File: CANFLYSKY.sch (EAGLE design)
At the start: 47 parts, among them J1 USB_B_PTH, SW1 SWITCH-DPDT3, U1 MCP2551, X1 INPUT, X2 OUTPUT

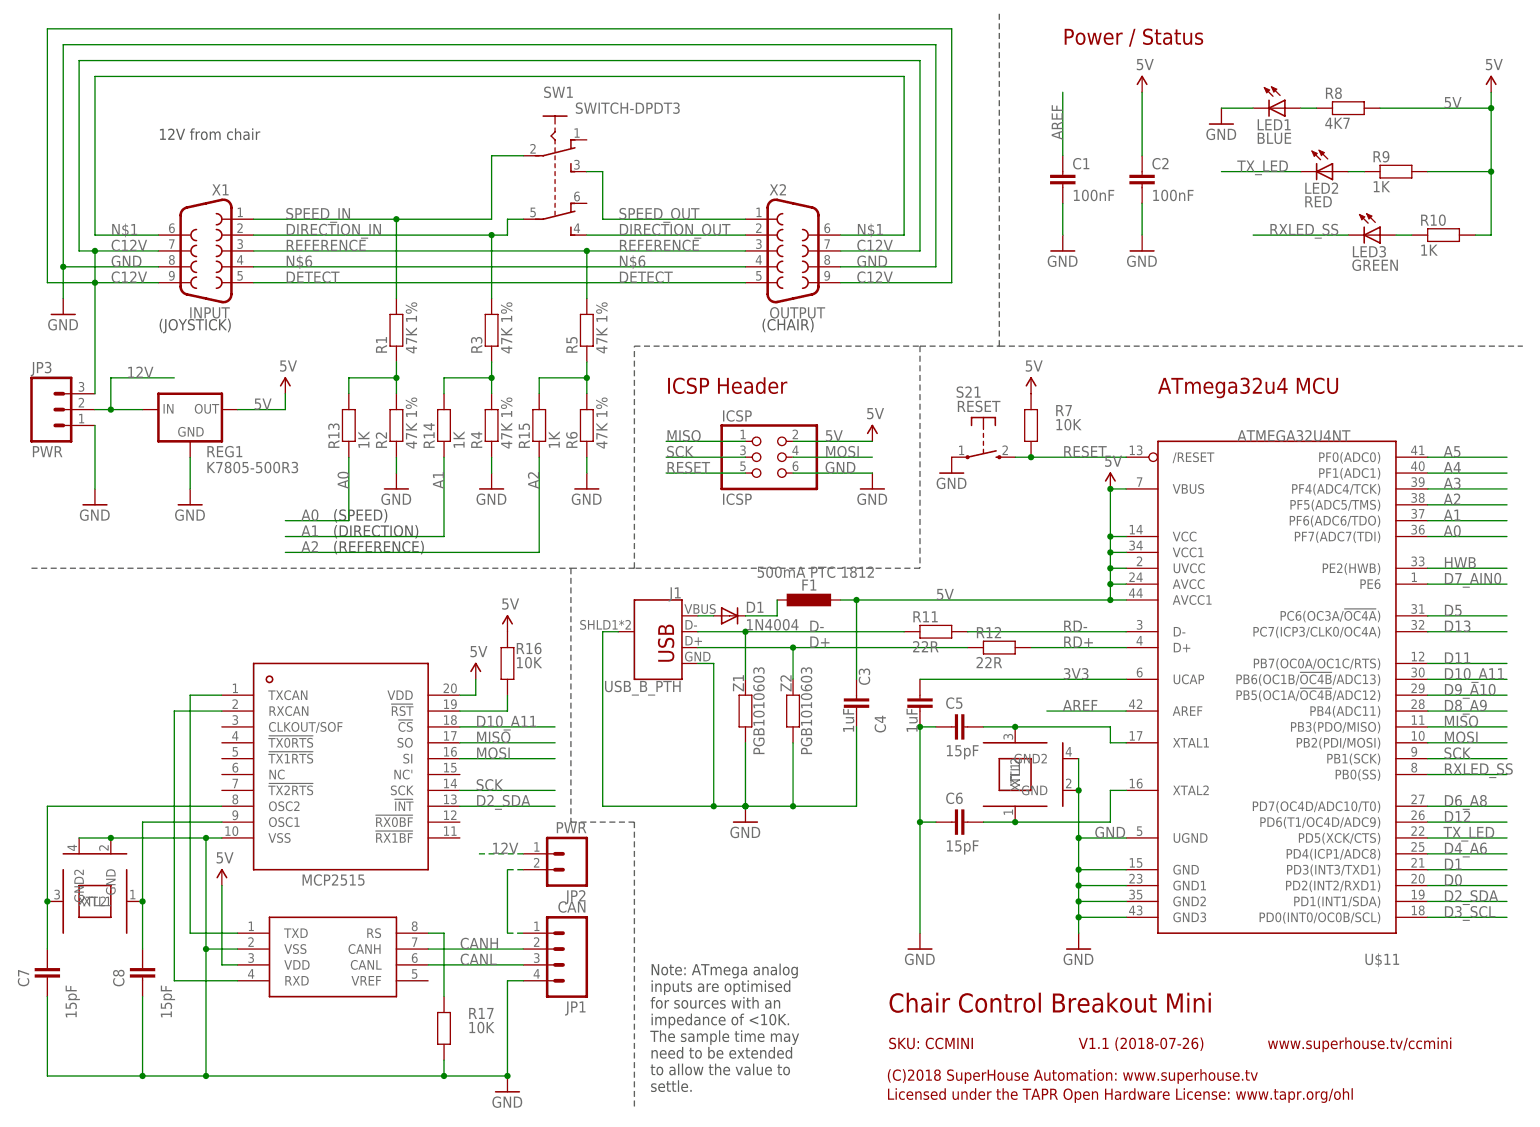
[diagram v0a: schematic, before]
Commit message: Removed unnecessary parts
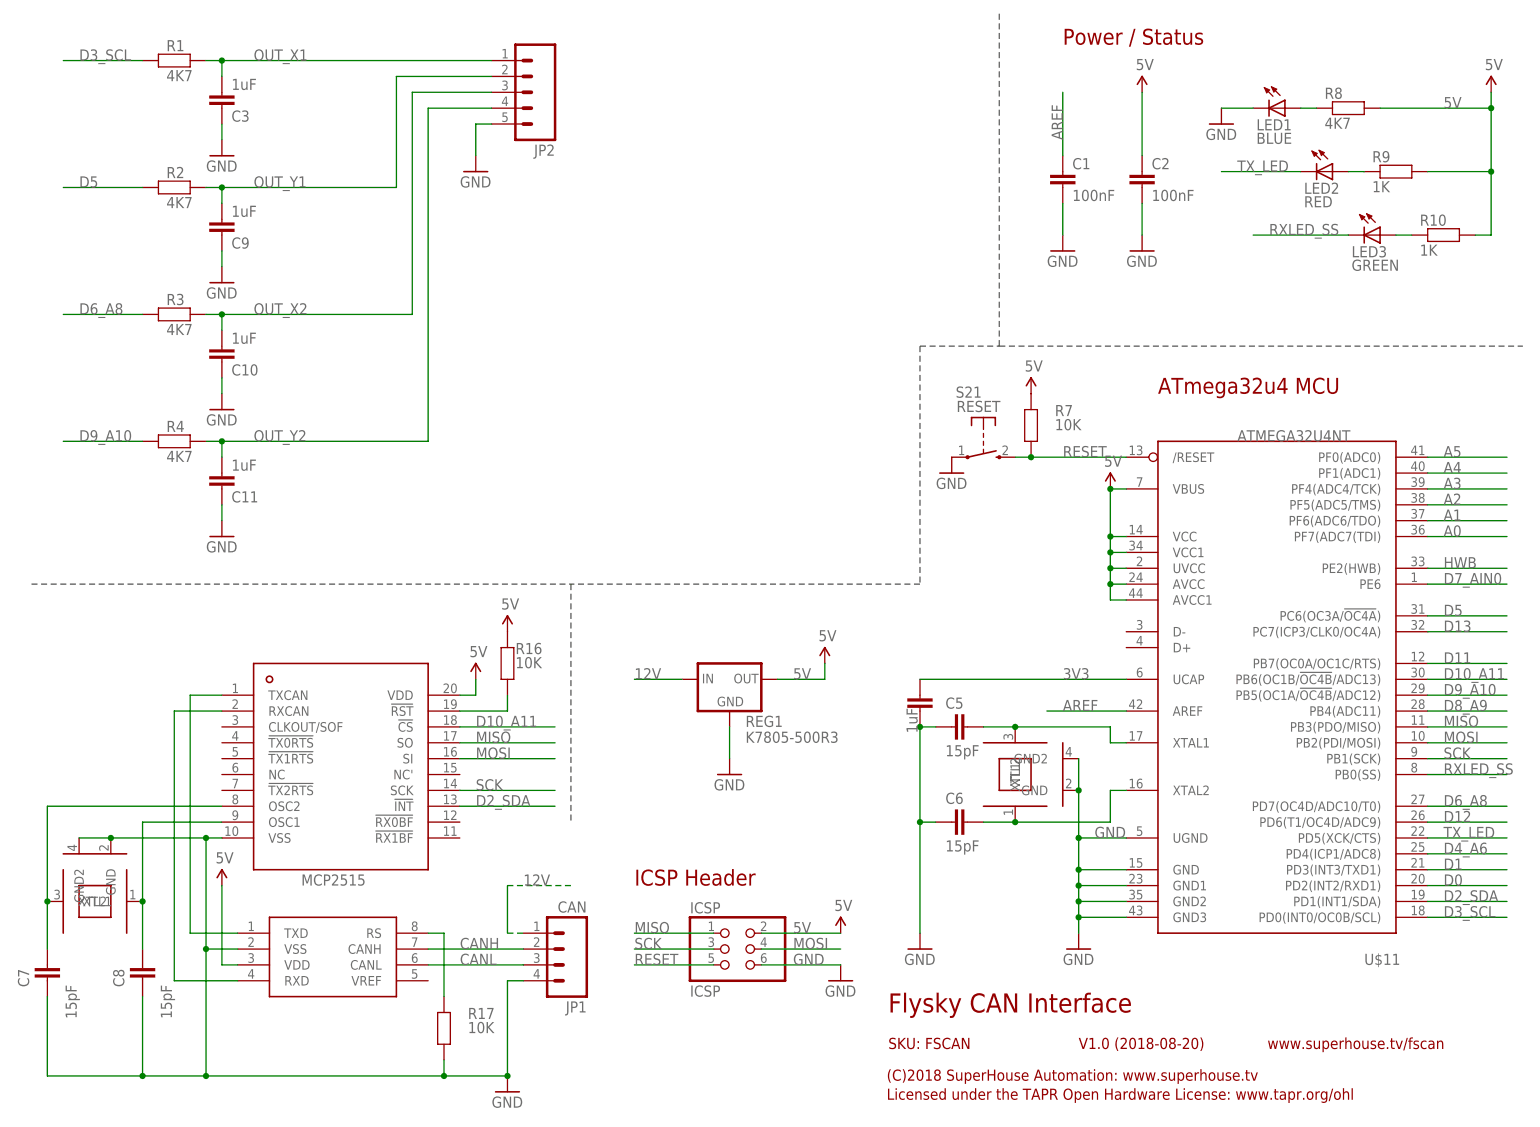
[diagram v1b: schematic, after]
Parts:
- removed D1: 1N4004, freetronics-jon:DIODESMB
- removed F1: 500mA PTC 1812, rcl:L-EUL1812
- removed J1: USB_B_PTH, SparkFun-Connectors:USB_B_PTH
- removed JP3: PWR, freetronics-jon:M03PTH
- removed R11, R12: 22R, freetronics-jon:RESISTOR0603
- removed R13, R14, R15: 1K, freetronics-jon:RESISTOR0603
- removed R5, R6: 47K 1%, freetronics-jon:RESISTOR0603
- removed SW1: SWITCH-DPDT3, freetronics-jon:SWITCH-DPDT3
- removed X1: INPUT, SparkFun-Connectors:DB9MALE
- removed X2: OUTPUT, SparkFun-Connectors:DB9FEMALE
- removed Z1, Z2: PGB1010603, freetronics-master-v1.1:RESISTOR0603
- added C10, C11, C9: 1uF, freetronics-master-v1.1:CAP0603
- JP2: value PWR -> (none); device freetronics-jon:M02PTH -> freetronics-jon:M05PTH
- R1, R2, R3, R4: value 47K 1% -> 4K7; device freetronics-jon:RESISTOR0603 -> freetronics-master-v1.1:RESISTOR0603
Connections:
- removed net C12V: JP3.3, X1.7, X1.9, X2.7, X2.9
- removed net D+: J1.D+, R12.1, Z2.2
- removed net D-: J1.D-, R11.1, Z1.2
- removed net DETECT: X1.5, X2.5
- removed net DIRECTION_IN: R3.2, SW1.5, X1.2
- removed net DIRECTION_OUT: SW1.4, X2.2
- removed net N$1: X1.6, X2.6
- removed net N$15: JP1.1, JP2.2
- removed net N$17: D1.C, F1.1
- removed net N$2: R1.1, R13.2, R2.2
- removed net N$3: R14.2, R3.1, R4.2
- removed net N$4: R15.2, R5.1, R6.2
- removed net N$6: X1.4, X2.4
- removed net RD+: R12.2, U$11.D+
- removed net RD-: R11.2, U$11.D-
- removed net REFERENCE: R5.2, X1.3, X2.3
- removed net SPEED_IN: R1.2, SW1.2, X1.1
- removed net SPEED_OUT: SW1.3, X2.1
- removed net USB+: D1.A, J1.VBUS
- new net OUT_X1: C3.1, JP2.1, R1.2
- new net OUT_X2: C10.1, JP2.3, R3.2
- new net OUT_Y1: C9.1, JP2.2, R2.2
- new net OUT_Y2: C11.1, JP2.4, R4.2
- net 12V: now also JP1.1; no longer JP2.1, JP3.2
- net 5V: no longer C3.1, F1.2
- net A0: no longer R13.1
- net A1: no longer R14.1
- net A2: no longer R15.1
- net D3_SCL: now also R1.1
- net D5: now also R2.1
- net D6_A8: now also R3.1
- net D9_A10: now also R4.1
- net GND: now also C10.2, C11.2, C9.2, JP2.5; no longer J1.GND, J1.SHIELD, JP3.1, R2.1, R4.1, R6.1, X1.8, X2.8, Z1.1, Z2.1
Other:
- note added: "Flysky CAN Interface"
- note added: "SKU: FSCAN"
- note added: "V1.0 (2018-08-20)"
- note added: "www.superhouse.tv/fscan"
- note removed: "(CHAIR)"
- note removed: "(DIRECTION)"
- note removed: "(JOYSTICK)"
- note removed: "(REFERENCE)"
- note removed: "(SPEED)"
- note removed: "12V from chair"
- note removed: "Chair Control Breakout Mini"
- note removed: "Note: ATmega analog inputs are optimised for sources with an impedance of <10K. The sample time may need to be extended to allow the value to settle."
- note removed: "SKU: CCMINI"
- note removed: "V1.1 (2018-07-26)"
- note removed: "www.superhouse.tv/ccmini"
- moved on the sheet: C3, ICSP, R1, R2, R3, R4, REG1

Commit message: Completed initial routing
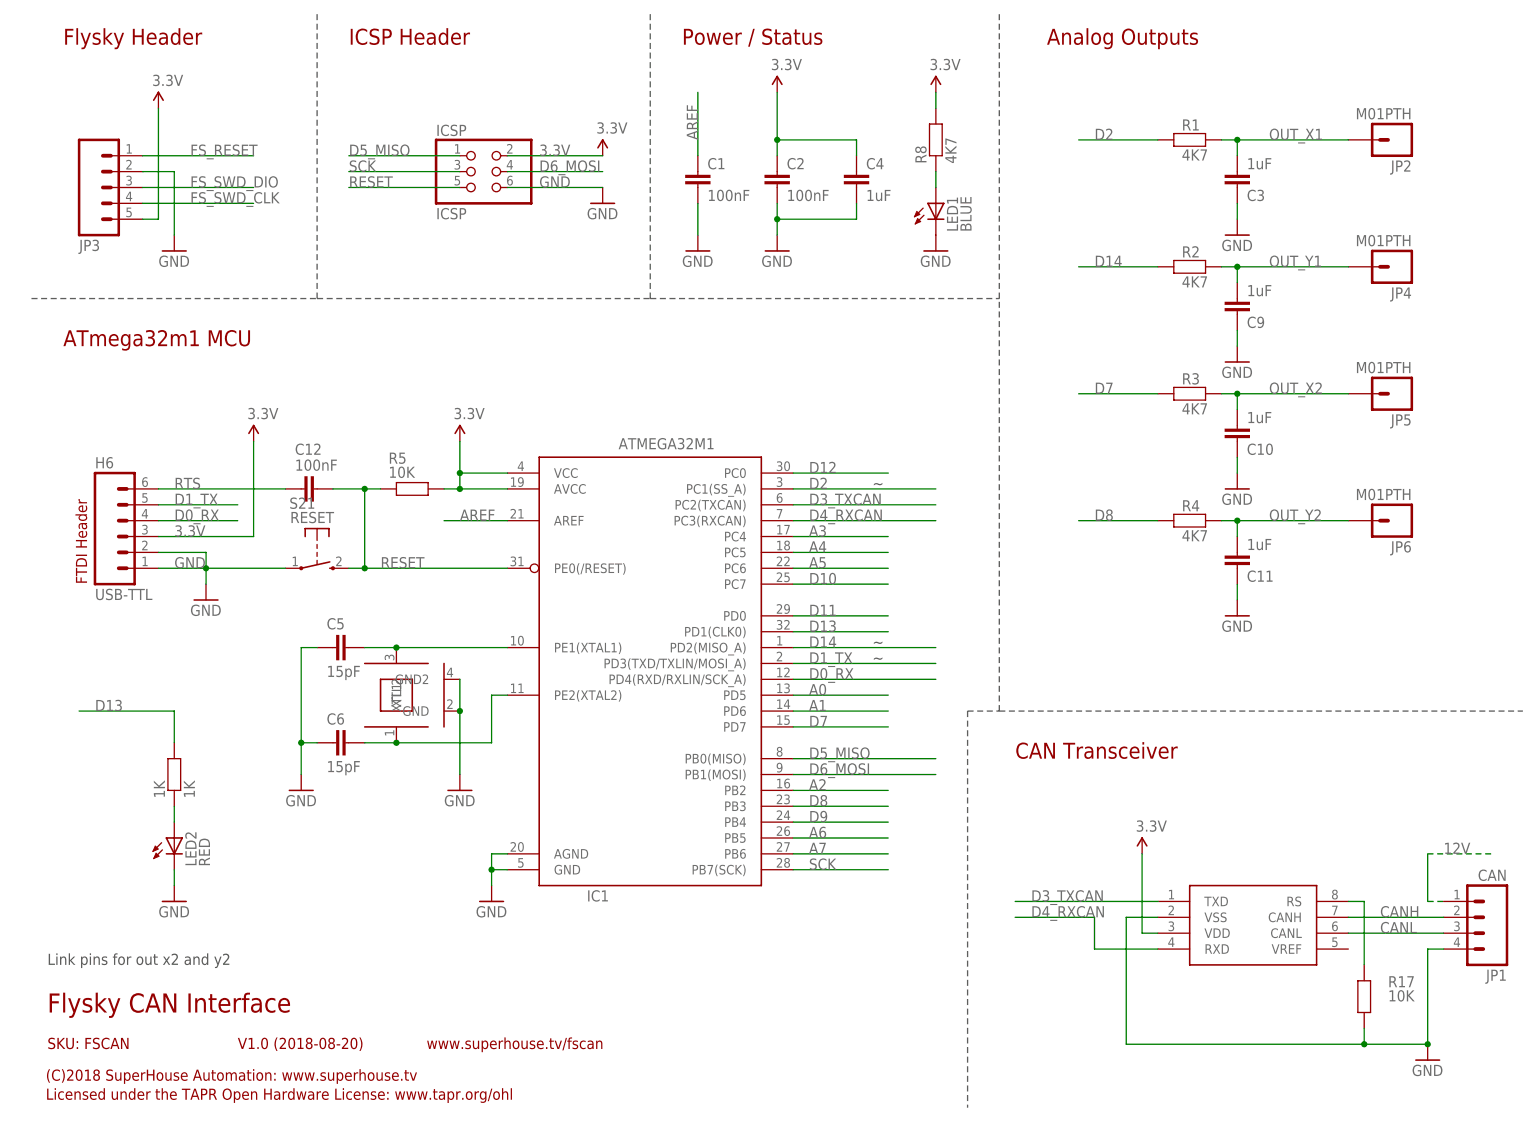
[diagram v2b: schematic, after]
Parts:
- removed C7, C8: 15pF, freetronics-master-v1.1:CAP0603
- removed LED3: GREEN, freetronics-jon:LED0603
- removed R10, R9: 1K, freetronics-jon:RESISTOR0603
- removed R16, R7: 10K, freetronics-master-v1.1:RESISTOR0603
- removed REG1: K7805-500R3, freetronics-jon:K78XX-500R3
- removed U$11: ATMEGA32U4NT, freetronics-jon:ATMEGA32U4NT
- removed U$4: MCP2515, MCP2515:MCP2515
- removed XTL2: 16MHz, freetronics-jon:CRYSTAL-GND3X2
- added 1K: 1K, freetronics-jon:RESISTOR0603
- added C12: 100nF, freetronics-master-v1.1:CAP0603
- added H6: USB-TTL, freetronics:M06SIP
- added IC1: ATMEGA32M1, freetronics-jon:ATMEGA32M1
- added JP3: (no value), freetronics-jon:M05PTH
- added JP4, JP5, JP6: M01PTH, freetronics-jon:M01PTH
- added R5: 10K, freetronics-master-v1.1:RESISTOR0603
- JP2: value (none) -> M01PTH; device freetronics-jon:M05PTH -> freetronics-jon:M01PTH
- XTL1: value 16MHz -> 8MHz
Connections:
- removed net 3V3: C4.2, U$11.UCAP
- removed net 5V: C2.1, ICSP.2, R10.2, R16.2, R7.2, R8.2, R9.2, REG1.OUT, U$11.AVCC, U$11.AVCC1, U$11.UVCC, U$11.VBUS, U$11.VCC, U$11.VCC1, U$4.VDD, U1.VDD
- removed net D0: U$11.PD2(INT2/RXD1)
- removed net D1: U$11.PD3(INT3/TXD1)
- removed net D10_A11: U$11.PB6(OC1B/!OC4B!/ADC13), U$4.!CS
- removed net D2_SDA: U$11.PD1(INT1/SDA), U$4.!INT
- removed net D3_SCL: R1.1, U$11.PD0(INT0/OC0B/SCL)
- removed net D4_A6: U$11.PD4(ICP1/ADC8)
- removed net D5: R2.1, U$11.PC6(OC3A/!OC4A!)
- removed net D6_A8: R3.1, U$11.PD7(OC4D/ADC10/T0)
- removed net D7_AIN0: U$11.PE6
- removed net D8_A9: U$11.PB4(ADC11)
- removed net D9_A10: R4.1, U$11.PB5(OC1A/!OC4B!/ADC12)
- removed net HWB: U$11.PE2(HWB)
- removed net MISO: ICSP.1, U$11.PB3(PDO/MISO), U$4.SO
- removed net MOSI: ICSP.4, U$11.PB2(PDI/MOSI), U$4.SI
- removed net N$10: R16.1, U$4.!RST
- removed net N$13: U$4.RXCAN, U1.RXD
- removed net N$14: C8.2, U$4.OSC1, XTL2.XTL1
- removed net N$18: C7.2, U$4.OSC2, XTL2.XTL2
- removed net N$7: LED2.A, R9.1
- removed net N$8: LED3.A, R10.1
- removed net N$9: U$4.TXCAN, U1.TXD
- removed net RXLED_SS: LED3.C, U$11.PB0(SS)
- removed net TX_LED: LED2.C, U$11.PD5(XCK/CTS)
- new net 3.3V: C2.1, C4.1, H6.3, IC1.AVCC, IC1.VCC, ICSP.2, JP3.5, R5.1, R8.2, U1.VDD
- new net A6: IC1.PB5
- new net A7: IC1.PB6
- new net D0_RX: H6.4, IC1.PD4(RXD/RXLIN/SCK_A)
- new net D10: IC1.PC7
- new net D14: IC1.PD2(MISO_A), R2.1
- new net D1_TX: H6.5, IC1.PD3(TXD/TXLIN/MOSI_A)
- new net D2: IC1.PC1(SS_A), R1.1
- new net D3_TXCAN: IC1.PC2(TXCAN), U1.TXD
- new net D4_RXCAN: IC1.PC3(RXCAN), U1.RXD
- new net D5_MISO: IC1.PB0(MISO), ICSP.1
- new net D6_MOSI: IC1.PB1(MOSI), ICSP.4
- new net D7: IC1.PD7, R3.1
- new net D8: IC1.PB3, R4.1
- new net D9: IC1.PB4
- new net FS_RESET: JP3.1
- new net FS_SWD_CLK: JP3.4
- new net FS_SWD_DIO: JP3.3
- new net N$1: 1K.1, LED2.A
- new net RTS: C12.1, H6.6
- net 12V: no longer REG1.IN
- net A0: now also IC1.PD5; no longer U$11.PF7(ADC7(TDI)
- net A1: now also IC1.PD6; no longer U$11.PF6(ADC6/TDO)
- net A2: now also IC1.PB2; no longer U$11.PF5(ADC5/TMS)
- net A3: now also IC1.PC4; no longer U$11.PF4(ADC4/TCK)
- net A4: now also IC1.PC5; no longer U$11.PF1(ADC1)
- net A5: now also IC1.PC6; no longer U$11.PF0(ADC0)
- net AREF: now also IC1.AREF; no longer U$11.AREF
- net D11: now also IC1.PD0; no longer U$11.PB7(OC0A/OC1C/RTS)
- net D12: now also IC1.PC0; no longer U$11.PD6(T1/OC4D/ADC9)
- net D13: now also 1K.2, IC1.PD1(CLK0); no longer U$11.PC7(ICP3/CLK0/OC4A)
- net GND: now also C4.2, H6.1, H6.2, IC1.AGND, IC1.GND, JP3.2, LED2.C; no longer C4.1, C7.1, C8.1, JP2.5, REG1.GND, U$11.GND, U$11.GND1, U$11.GND2, U$11.GND3, U$11.UGND, U$4.VSS, XTL2.GND, XTL2.GND2
- net N$11: now also IC1.PE1(XTAL1); no longer U$11.XTAL1
- net N$12: now also IC1.PE2(XTAL2); no longer U$11.XTAL2
- net OUT_X2: now also JP5.1; no longer JP2.3
- net OUT_Y1: now also JP4.1; no longer JP2.2
- net OUT_Y2: now also JP6.1; no longer JP2.4
- net RESET: now also C12.2, IC1.PE0(/RESET), R5.2; no longer R7.1, U$11./RESET
- net SCK: now also IC1.PB7(SCK); no longer U$11.PB1(SCK), U$4.SCK
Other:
- note added: "ATmega32m1 MCU"
- note added: "Analog Outputs"
- note added: "CAN Transceiver"
- note added: "FTDI Header"
- note added: "Flysky Header"
- note added: "Link pins for out x2 and y2"
- note added: "~"
- note removed: "ATmega32u4 MCU"
- moved on the sheet: C1, C10, C11, C2, C3, C5, C6, C9, ICSP, JP1, LED1, LED2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

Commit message: Finished routing
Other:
- note added: "Flysky FS-i6 CAN Interface"
- note added: "SKU: FSI6CAN"
- note added: "www.superhouse.tv/fsi6can"
- note removed: "Flysky CAN Interface"
- note removed: "SKU: FSCAN"
- note removed: "www.superhouse.tv/fscan"
